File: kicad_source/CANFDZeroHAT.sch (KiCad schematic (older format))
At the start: 1 part, among them CN1 RASPI-IO

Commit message: generated schematic and layout
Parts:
- added C1, C4: 100nF, capacitors:C_0603, symbol devices:C_0603
- added C2, C3: 22pF, capacitors:C_0603, symbol devices:C_0603
- added CN2: CONN_01X04, CON_wuerth:WR-TBL_691210910004, symbol mechanical-connectors:CONN_01X04
- added CN3, CN4: GH_SM04B-GHS-TB, Connector_JST:JST_GH_SM04B-GHS-TB_1x04-1MP_P1.25mm_Horizontal, symbol mechanical-connectors:CONN_01X04
- added D1: DNI, diodes:SOD-123, symbol devices:D_Schottky_Small
- added L1: Label, labels:generationmake_small_solder, symbol devices:Label
- added L2: Label, labels:generationmake_logo, symbol devices:Label
- added R1: 0R, resistors:R_0603, symbol devices:R_0603
- added R2: DNI, resistors:R_0603, symbol devices:R_0603
- added R3, R5: 10k, resistors:R_0603, symbol devices:R_0603
- added R4: 120R, resistors:R_0603, symbol devices:R_0603
- added SW1: JS202011JCQN, mechanical-switches:CK_JS202011JCQN, symbol devices:SWITCH_SMALL
- added U1: MCP2517FD, SOIC:SOIC-14_3.9x8.7mm_Pitch1.27mm, symbol IC_transceiver_can:MCP2517FD
- added U2: SN65HVD232, SOIC:SOIJ-8_5.3x5.3mm_Pitch1.27mm, symbol CAN-transceiver:SN65HVD232
- added Y1: RH100-20.000-20-3030-TR, crystals:Crystal_SMD_3.2x2.5mm_4Pad, symbol devices:Crystal_SMD_4Pad
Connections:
- net labels added: CANH, CANL, CANVCC, CAN_RX, CAN_TX, MCP2517_CS, MCP2517_INT, OSC1, OSC2
- wire segments 33 -> 109
- no-connect marks 0 -> 6
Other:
- note added: "20 MHz"
- note added: "CAN in"
- note added: "CAN out"
- note added: "UAVCAN Dronecode connectors"

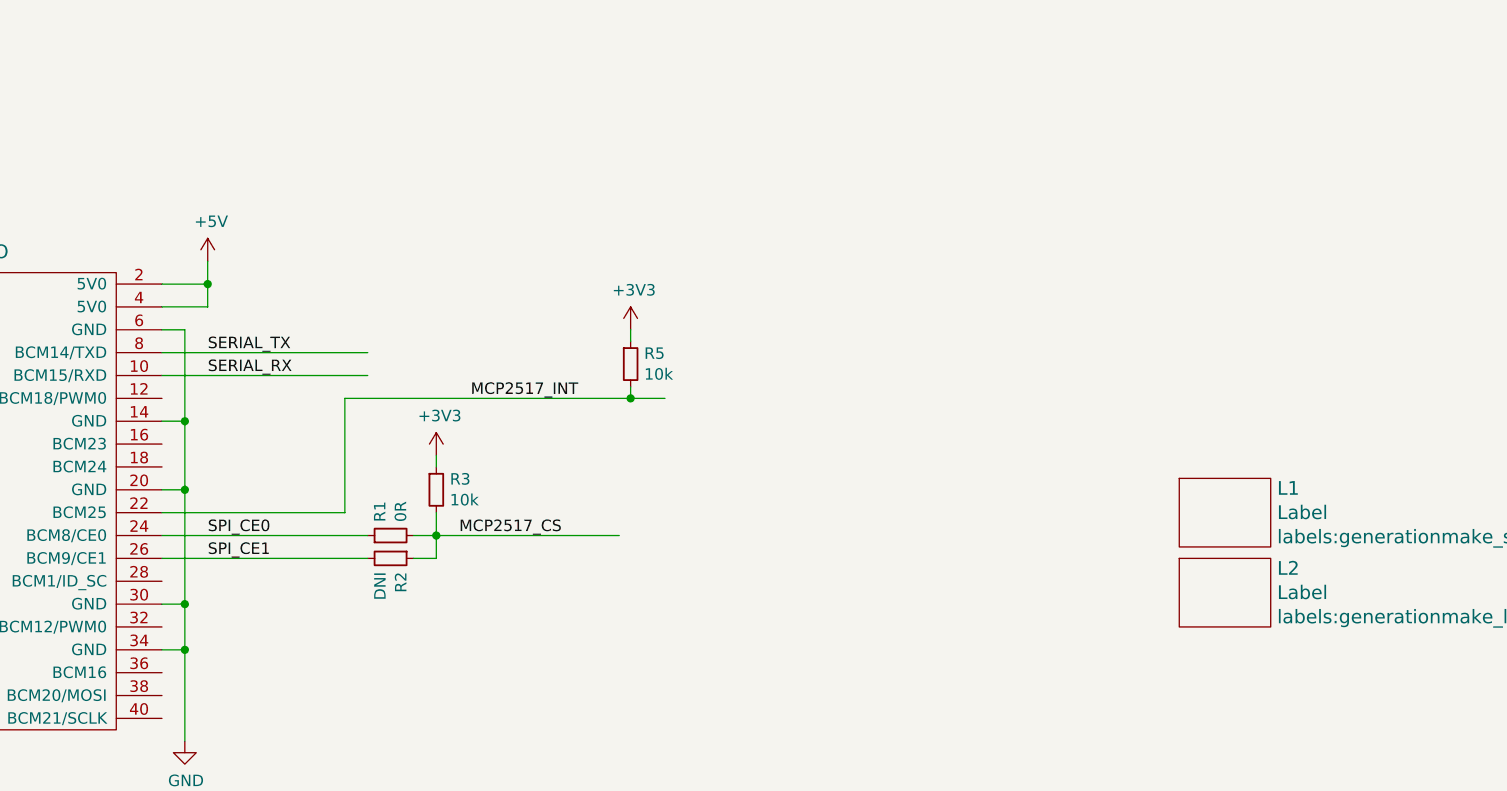
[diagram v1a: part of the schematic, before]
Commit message: added option resistors, updated layout
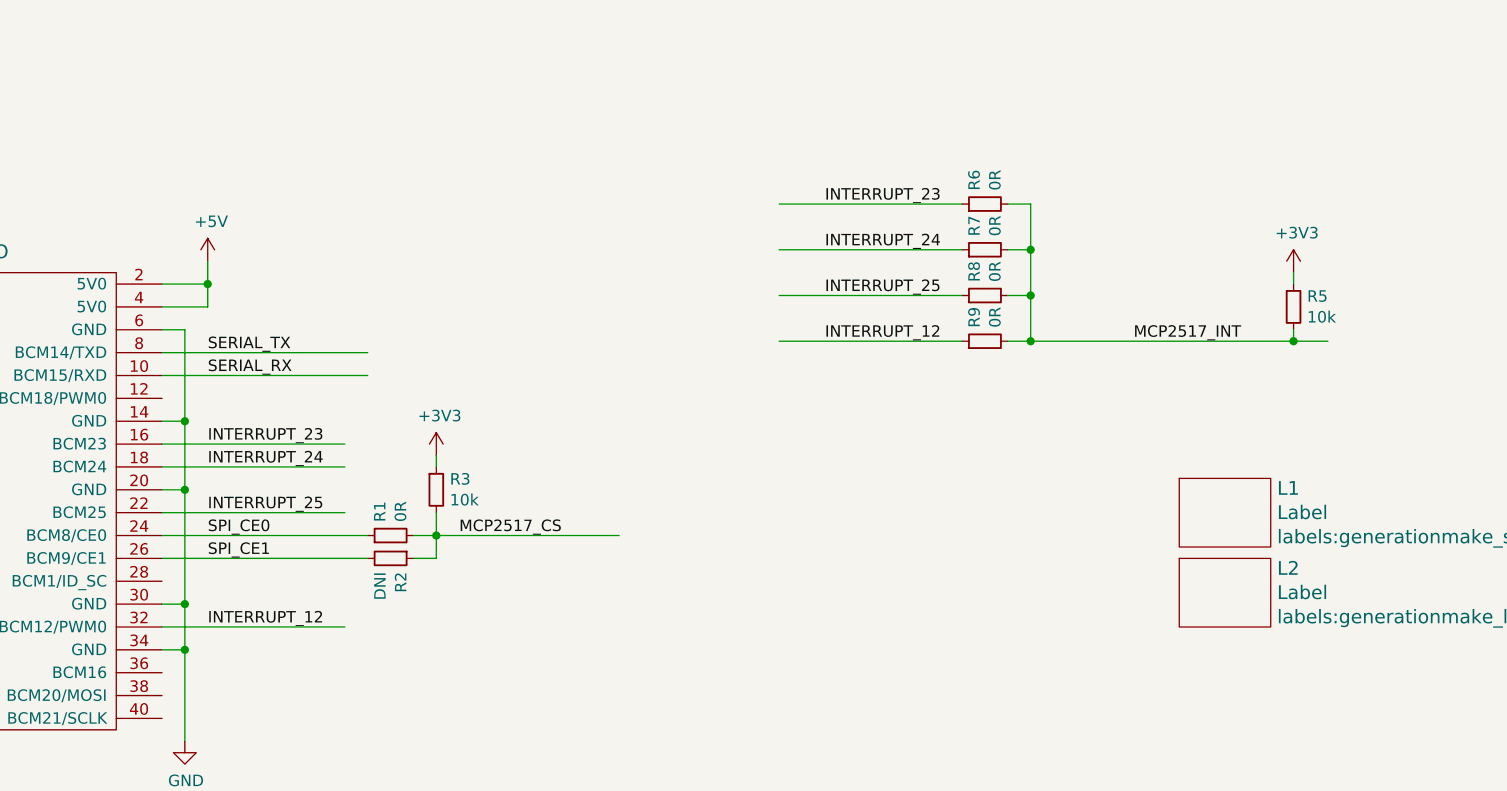
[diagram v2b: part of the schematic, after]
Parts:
- added R6, R7, R8, R9: 0R, resistors:R_0603, symbol devices:R_0603
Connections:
- net labels added: INTERRUPT_12, INTERRUPT_23, INTERRUPT_24, INTERRUPT_25
- wire segments 109 -> 122
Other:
- moved on the sheet: R5
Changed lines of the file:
@@
 	0    1    1    0
 $EndComp
-Text Label 5950 5450 0    50   ~ 0
+Text Label 8850 5200 0    50   ~ 0
 MCP2517_INT
 $Comp
 L devices:R_0603 R5
 U 1 1 5FD88AEB
-P 6650 5300
-F 0 "R5" H 6709 5346 50  0000 L CNN
-F 1 "10k" H 6709 5255 50  0000 L CNN
-F 2 "resistors:R_0603" H 6650 5150 50  0001 C CNN
-F 3 "" H 6650 5300 50  0000 C CNN
-	1    6650 5300
+P 9550 5050
+F 0 "R5" H 9609 5096 50  0000 L CNN
+F 1 "10k" H 9609 5005 50  0000 L CNN
+F 2 "resistors:R_0603" H 9550 4900 50  0001 C CNN
+F 3 "" H 9550 5050 50  0000 C CNN
+	1    9550 5050
 	1    0    0    -1
 $EndComp
@@
 L power-supply:+3V3 #PWR011
 U 1 1 5FD88AF1
-P 6650 5150
-F 0 "#PWR011" H 6650 5000 50  0001 C CNN
-F 1 "+3V3" H 6665 5323 50  0000 C CNN
-F 2 "" H 6650 5150 50  0000 C CNN
-F 3 "" H 6650 5150 50  0000 C CNN
-	1    6650 5150
+P 9550 4900
+F 0 "#PWR011" H 9550 4750 50  0001 C CNN
+F 1 "+3V3" H 9565 5073 50  0000 C CNN
+F 2 "" H 9550 4900 50  0000 C CNN
+F 3 "" H 9550 4900 50  0000 C CNN
+	1    9550 4900
 	1    0    0    -1
 $EndComp
 Wire Wire Line
-	6650 5150 6650 5200
+	9550 4900 9550 4950
 Wire Wire Line
-	6650 5400 6650 5450
-Connection ~ 6650 5450
+	9550 5150 9550 5200
+Connection ~ 9550 5200
 Wire Wire Line
-	6650 5450 6800 5450
+	9550 5200 9700 5200
 Wire Wire Line
 	5700 6050 5800 6050
@@
 	4600 5950 5400 5950
 Wire Wire Line
-	5400 5950 5400 5450
-Wire Wire Line
-	5400 5450 6650 5450
+	8300 5200 8400 5200
 $Comp
 L power-supply:+5V #PWR?
@@
 	1    0    0    -1
 $EndComp
+Text Label 4800 5950 0    50   ~ 0
+INTERRUPT_25
+Wire Wire Line
+	4600 5750 5400 5750
+Text Label 4800 5750 0    50   ~ 0
+INTERRUPT_24
+Wire Wire Line
+	4600 5650 5400 5650
+Text Label 4800 5650 0    50   ~ 0
+INTERRUPT_23
+Wire Wire Line
+	4600 6450 5400 6450
+Text Label 4800 6450 0    50   ~ 0
+INTERRUPT_12
+Wire Wire Line
+	7300 5000 8100 5000
+Text Label 7500 5000 0    50   ~ 0
+INTERRUPT_25
+Wire Wire Line
+	7300 4800 8100 4800
+Text Label 7500 4800 0    50   ~ 0
+INTERRUPT_24
+Wire Wire Line
+	7300 4600 8100 4600
+Text Label 7500 4600 0    50   ~ 0
+INTERRUPT_23
+Wire Wire Line
+	7300 5200 8100 5200
+Text Label 7500 5200 0    50   ~ 0
+INTERRUPT_12
+$Comp
+L devices:R_0603 R?
+U 1 1 5FDE9CB4
+P 8200 5200
+AR Path="/5FD58A5B/5FDE9CB4" Ref="R?"  Part="1"
+AR Path="/5FDE9CB4" Ref="R9"  Part="1"
+F 0 "R9" H 8259 5246 50  0000 L CNN
+F 1 "0R" H 8259 5155 50  0000 L CNN
+F 2 "resistors:R_0603" H 8200 5050 50  0001 C CNN
+F 3 "" H 8200 5200 50  0000 C CNN
+	1    8200 5200
+	0    -1   -1   0
+$EndComp
+$Comp
+L devices:R_0603 R?
+U 1 1 5FDEA10B
+P 8200 5000
+AR Path="/5FD58A5B/5FDEA10B" Ref="R?"  Part="1"
+AR Path="/5FDEA10B" Ref="R8"  Part="1"
+F 0 "R8" H 8259 5046 50  0000 L CNN
+F 1 "0R" H 8259 4955 50  0000 L CNN
+F 2 "resistors:R_0603" H 8200 4850 50  0001 C CNN
+F 3 "" H 8200 5000 50  0000 C CNN
+	1    8200 5000
+	0    -1   -1   0
+$EndComp
+$Comp
+L devices:R_0603 R?
+U 1 1 5FDEA376
+P 8200 4800
+AR Path="/5FD58A5B/5FDEA376" Ref="R?"  Part="1"
+AR Path="/5FDEA376" Ref="R7"  Part="1"
+F 0 "R7" H 8259 4846 50  0000 L CNN
+F 1 "0R" H 8259 4755 50  0000 L CNN
+F 2 "resistors:R_0603" H 8200 4650 50  0001 C CNN
+F 3 "" H 8200 4800 50  0000 C CNN
+	1    8200 4800
+	0    -1   -1   0
+$EndComp
+$Comp
+L devices:R_0603 R?
+U 1 1 5FDEE754
+P 8200 4600
+AR Path="/5FD58A5B/5FDEE754" Ref="R?"  Part="1"
+AR Path="/5FDEE754" Ref="R6"  Part="1"
+F 0 "R6" H 8259 4646 50  0000 L CNN
+F 1 "0R" H 8259 4555 50  0000 L CNN
+F 2 "resistors:R_0603" H 8200 4450 50  0001 C CNN
+F 3 "" H 8200 4600 50  0000 C CNN
+	1    8200 4600
+	0    -1   -1   0
+$EndComp
+Wire Wire Line
+	8300 4600 8400 4600
+Wire Wire Line
+	8400 4600 8400 4800
+Connection ~ 8400 5200
+Wire Wire Line
+	8400 5200 9550 5200
+Wire Wire Line
+	8300 5000 8400 5000
+Connection ~ 8400 5000
+Wire Wire Line
+	8400 5000 8400 5200
+Wire Wire Line
+	8300 4800 8400 4800
+Connection ~ 8400 4800
+Wire Wire Line
+	8400 4800 8400 5000
 $EndSCHEMATC
